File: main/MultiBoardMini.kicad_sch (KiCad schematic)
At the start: 45 parts, among them J1 PB0, J2 PA10, J3 Conn_01x02_Male, J4 Conn_01x03, SW1 PF1, SW2 RESET, SW3 PF0, T1 PTS_1.5_2, T2 PTS_1.5_2, T3 PTS_1.5_2, U1 NUCLEO-F303K8, U3 M78AR5-1

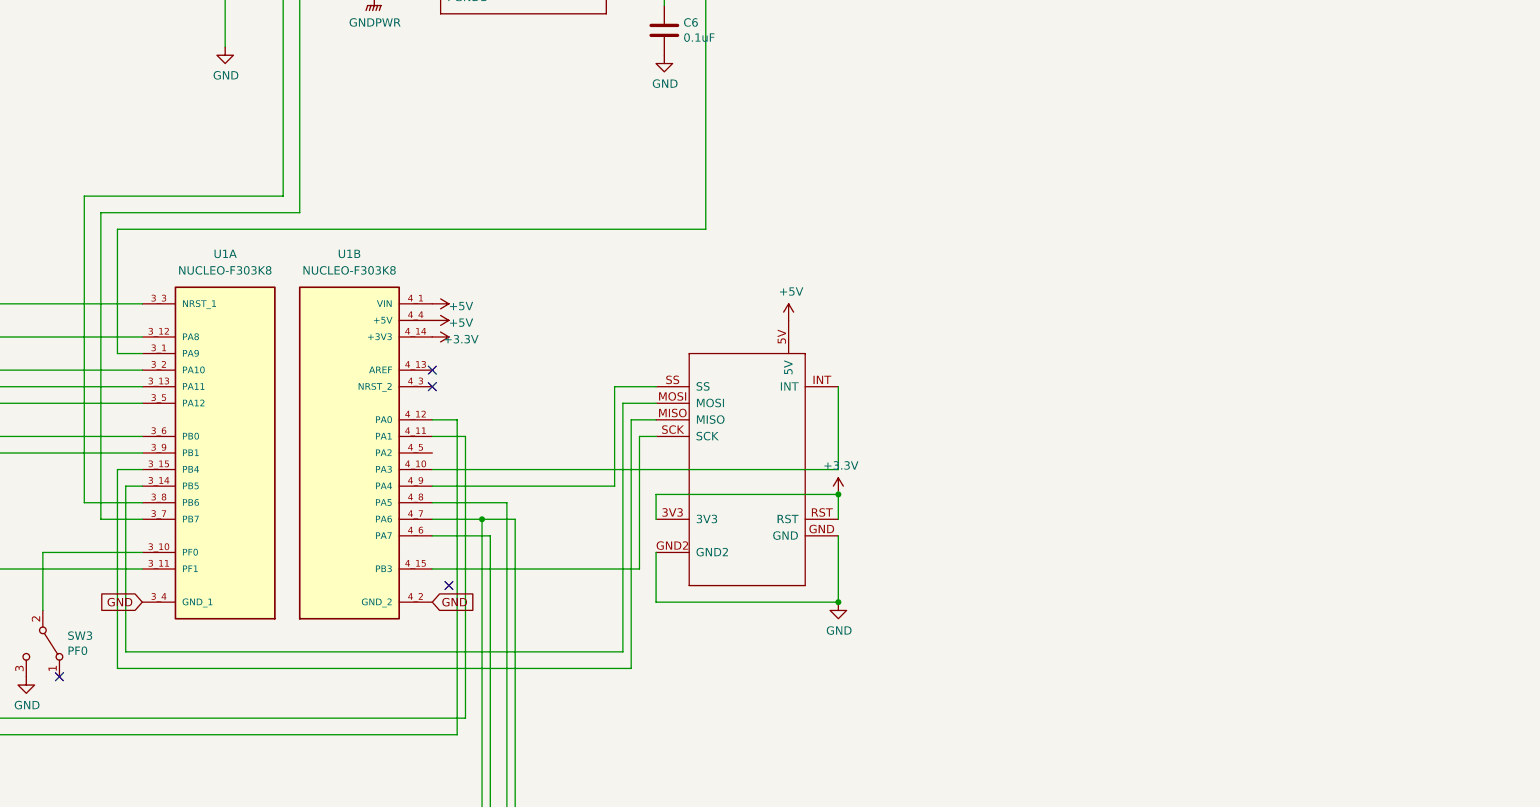
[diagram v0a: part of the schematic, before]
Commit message: 回路図にESP32モジュール追加
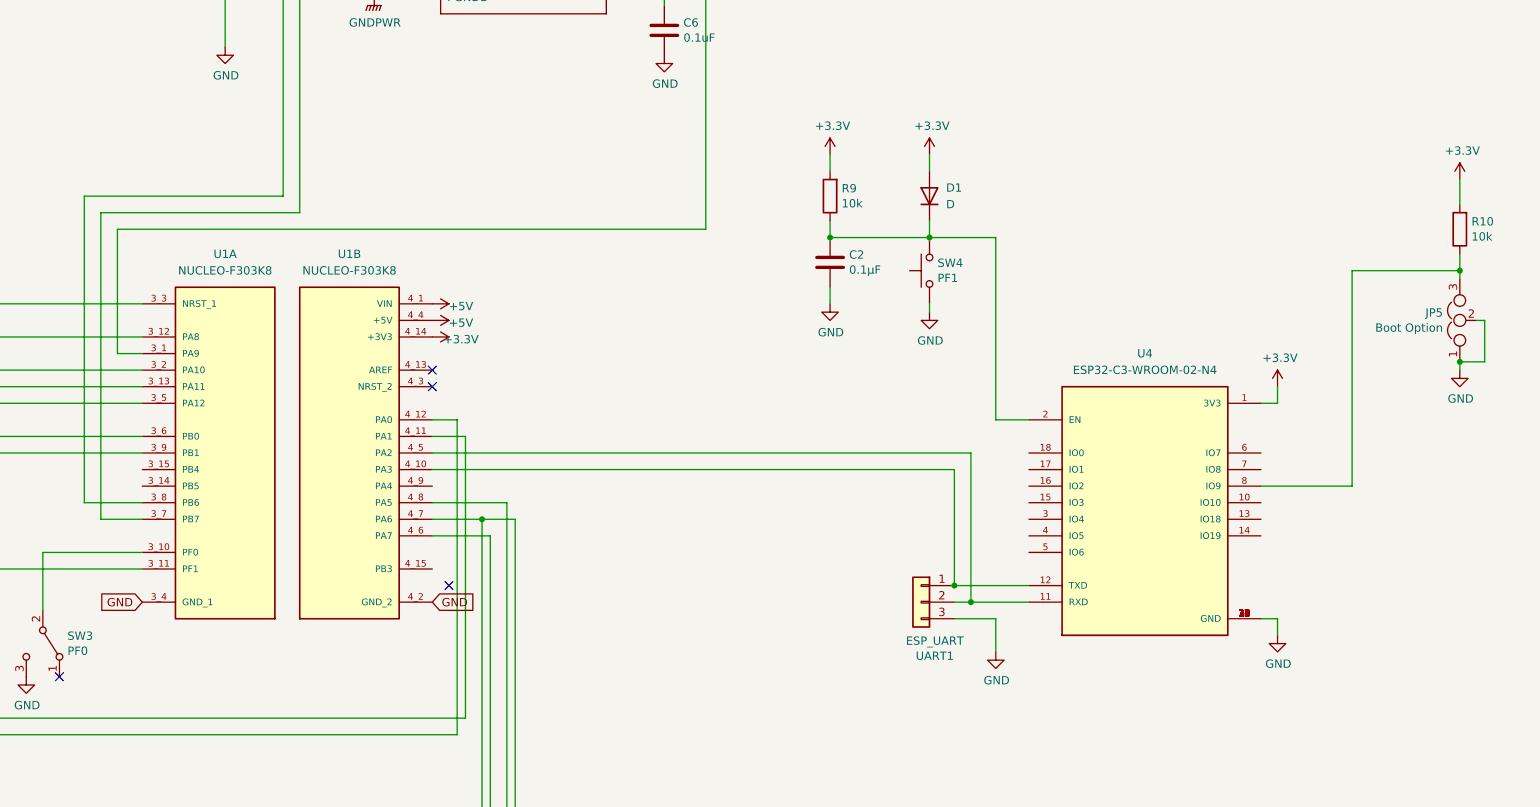
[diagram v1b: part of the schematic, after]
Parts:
- removed MINI-USB-HOST-SHIELD1: MINI-USB-HOST-SHIELD, mini-usb-host-shileld:MINI-USB-HOST-SHIELD, symbol mini-usb-host-shield:MINI-USB-HOST-SHIELD
- added C2: 0.1μF, Capacitor_SMD:C_0805_2012Metric, symbol Device:C
- added D1: D, symbol Device:D
- added JP5: Boot Option, Jumper:SolderJumper-3_P2.0mm_Open_TrianglePad1.0x1.5mm, symbol Device:Jumper_NC_Dual
- added R10, R9: 10k, Resistor_SMD:R_0603_1608Metric, symbol Device:R
- added SW4: PF1, Button_Switch_THT:SW_PUSH_6mm_H4.3mm, symbol Switch:SW_Push
- added U4: ESP32-C3-WROOM-02-N4, ESP32-C3-WROOM-02-N4:MODULE_ESP32-C3-WROOM-02-H4, symbol ESP32-C3-WROOM-02-N4:ESP32-C3-WROOM-02-N4
- added UART1: ESP_UART, Connector_JST:JST_XA_B03B-XASK-1_1x03_P2.50mm_Vertical, symbol Connector_Generic:Conn_01x03
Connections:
- net +3V3: now also D1.2 (A), R10.2, R9.2, U4.1 (3V3)
- net GND: now also C2.2, JP5.1, JP5.2, SW4.1, U4.19 (GND), U4.20 (GND), U4.21 (GND), U4.22 (GND), U4.23 (GND), U4.24 (GND), U4.25 (GND), U4.26 (GND), U4.27 (GND), U4.28 (GND), U4.29 (GND), U4.30 (GND), U4.31 (GND), U4.32 (GND), U4.33 (GND), U4.34 (GND), U4.35 (GND), U4.36 (GND), U4.37 (GND), U4.38 (GND), U4.39 (GND), U4.9 (GND), UART1.3 (Pin_3)
- net at U1.4_10 (PA3): now also U4.12 (TXD), UART1.1 (Pin_1)
- net at U1.4_5 (PA2): now also U4.11 (RXD), UART1.2 (Pin_2)
- new net: C2.1, D1.1 (K), R9.1, SW4.2, U4.2 (EN)
- new net: JP5.3, R10.1, U4.8 (IO9)

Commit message: 修正
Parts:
- added R11, R12: 10k, Resistor_SMD:R_0603_1608Metric, symbol Device:R
- D1: footprint (none) -> Diode_SMD:D_SOD-123F
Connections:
- net +3V3: now also D1.1 (K), U4.16 (IO2), U4.7 (IO8), R11.2, R12.2; no longer D1.2 (A)
- net GND: now also R11.1, R12.1
- net at C2.1, R9.1, SW4.2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: now also D1.2 (A); no longer D1.1 (K)
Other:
- moved on the sheet: C2, D1, JP5, R10, R9, SW4, U4, UART1
